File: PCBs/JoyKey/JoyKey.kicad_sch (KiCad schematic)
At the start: 3 parts, among them J1 OLED_DISPLAY, J3 Testpad wire hole1, U3 XIAO-RP2040-DIP

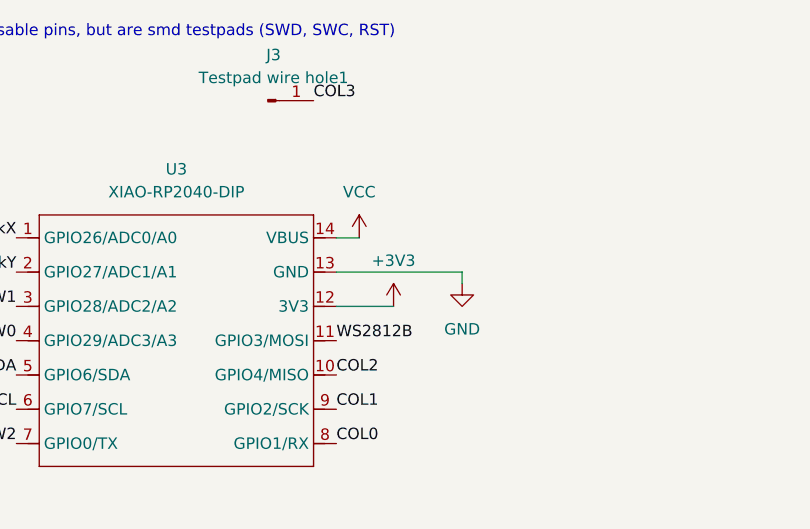
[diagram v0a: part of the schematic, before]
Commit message: Fixed ERC rules
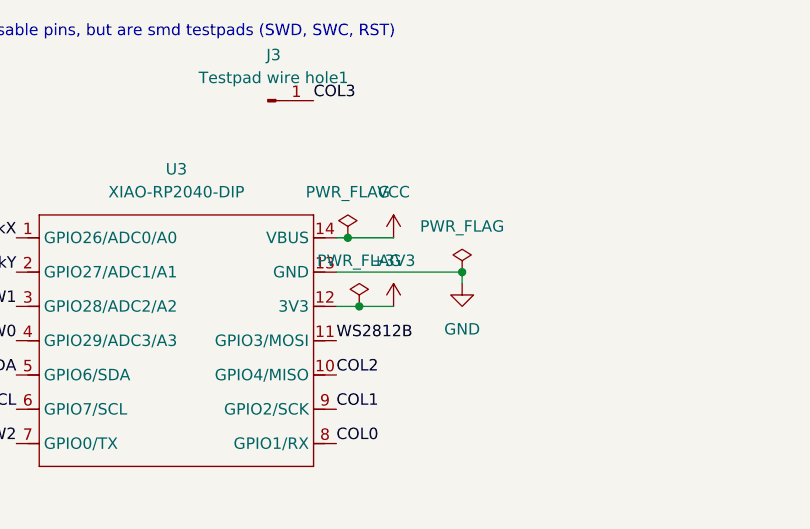
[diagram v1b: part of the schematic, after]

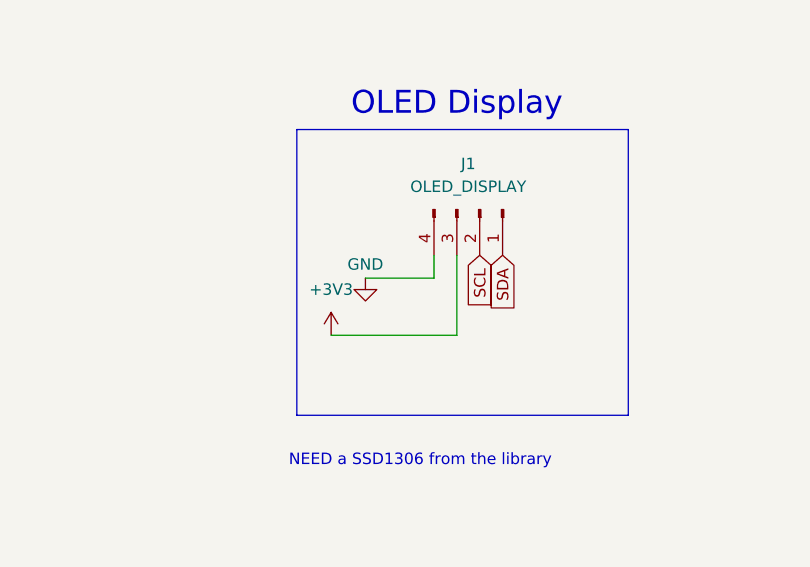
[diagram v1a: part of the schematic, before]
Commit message: Updated display to proper one
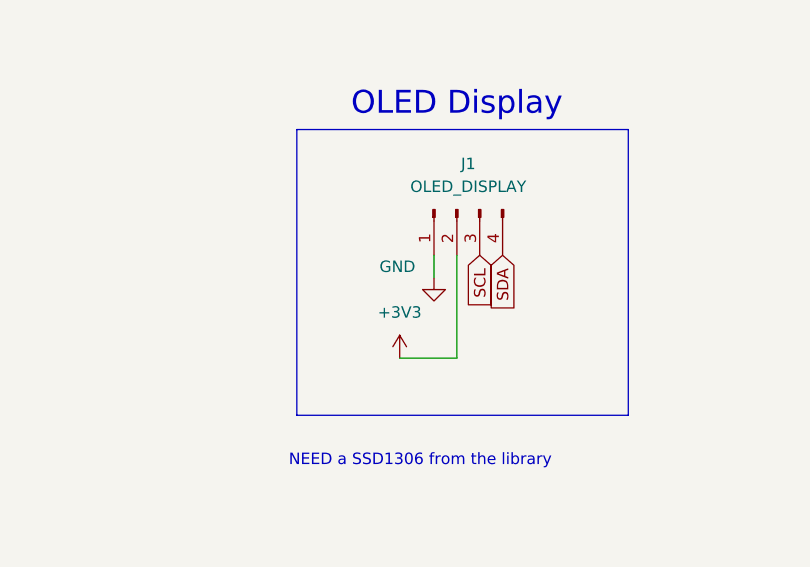
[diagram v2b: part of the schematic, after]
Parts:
- J1: footprint Display:Adafruit_SSD1306 -> SSD1306:SSD1306-OLED096-128x64
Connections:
- net +3V3: now also J1.2 (Pin_2); no longer J1.3 (Pin_3)
- net GND: now also J1.1 (Pin_1); no longer J1.4 (Pin_4)
- net SCL: now also J1.3 (Pin_3); no longer J1.2 (Pin_2)
- net SDA: now also J1.4 (Pin_4); no longer J1.1 (Pin_1)
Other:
- moved on the sheet: J1
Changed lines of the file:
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@@
 	(wire
 		(pts
-			(xy 196.85 66.04) (xy 210.82 66.04)
+			(xy 204.47 68.58) (xy 210.82 68.58)
 		)
 		(stroke
@@
 	(wire
 		(pts
-			(xy 200.66 59.69) (xy 208.28 59.69)
-		)
-		(stroke
-			(width 0)
-			(type default)
-		)
-	)
-	(wire
-		(pts
-			(xy 210.82 66.04) (xy 210.82 57.15)
+			(xy 210.82 68.58) (xy 210.82 57.15)
 		)
 		(stroke
@@
 	(symbol
 		(lib_id "power:GND")
-		(at 200.66 59.69 0)
+		(at 208.28 59.69 0)
 		(unit 1)
 		(exclude_from_sim no)
@@
 		(dnp no)
 		(property "Reference" "#PWR04"
-			(at 200.66 66.04 0)
+			(at 208.28 66.04 0)
 			(effects
 				(font
@@
 		)
 		(property "Value" "GND"
-			(at 200.66 58.166 0)
+			(at 204.216 58.42 0)
 			(effects
 				(font
@@
 		)
 		(property "Footprint" ""
-			(at 200.66 59.69 0)
+			(at 208.28 59.69 0)
 			(effects
 				(font
@@
 		)
 		(property "Datasheet" ""
-			(at 200.66 59.69 0)
+			(at 208.28 59.69 0)
 			(effects
 				(font
@@
 		)
 		(property "Description" "Power symbol creates a global label with name \"GND\" , ground"
-			(at 200.66 59.69 0)
+			(at 208.28 59.69 0)
 			(effects
 				(font
@@
 	(symbol
 		(lib_id "Connector:Conn_01x04_Pin")
-		(at 213.36 52.07 270)
+		(at 210.82 52.07 90)
+		(mirror x)
 		(unit 1)
 		(exclude_from_sim no)
@@
 			)
 		)
-		(property "Footprint" "Display:Adafruit_SSD1306"
-			(at 213.36 52.07 0)
+		(property "Footprint" "SSD1306:SSD1306-OLED096-128x64"
+			(at 210.82 52.07 0)
 			(effects
 				(font
@@
 		)
 		(property "Datasheet" "~"
-			(at 213.36 52.07 0)
+			(at 210.82 52.07 0)
 			(effects
 				(font
@@
 		)
 		(property "Description" "Generic connector, single row, 01x04, script generated"
-			(at 213.36 52.07 0)
+			(at 210.82 52.07 0)
 			(effects
 				(font
@@
 	(symbol
 		(lib_id "power:+3V3")
-		(at 196.85 66.04 0)
+		(at 204.47 68.58 0)
 		(unit 1)
 		(exclude_from_sim no)
@@
 		(fields_autoplaced yes)
 		(property "Reference" "#PWR05"
-			(at 196.85 69.85 0)
+			(at 204.47 72.39 0)
 			(effects
 				(font
@@
 		)
 		(property "Value" "+3V3"
-			(at 196.85 60.96 0)
+			(at 204.47 63.5 0)
 			(effects
 				(font
@@
 		)
 		(property "Footprint" ""
-			(at 196.85 66.04 0)
+			(at 204.47 68.58 0)
 			(effects
 				(font
@@
 		)
 		(property "Datasheet" ""
-			(at 196.85 66.04 0)
+			(at 204.47 68.58 0)
 			(effects
 				(font
@@
 		)
 		(property "Description" "Power symbol creates a global label with name \"+3V3\""
-			(at 196.85 66.04 0)
-			(effects
-				(font
+			(at 204.47 68.58 0)
+			(effects
+				(font

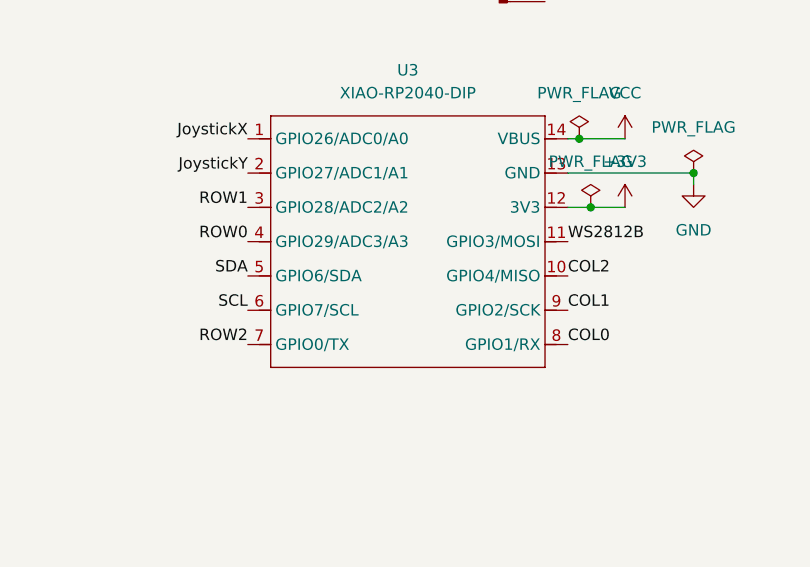
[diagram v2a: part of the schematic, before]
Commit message: Re-arranged matrix to have L-shaped clusters
Based on my horizontal layout I really have a 6*2 matrix, however the most switches for the least pins is actually a 4*3. So, I have to great creative with my routing to make it fit.
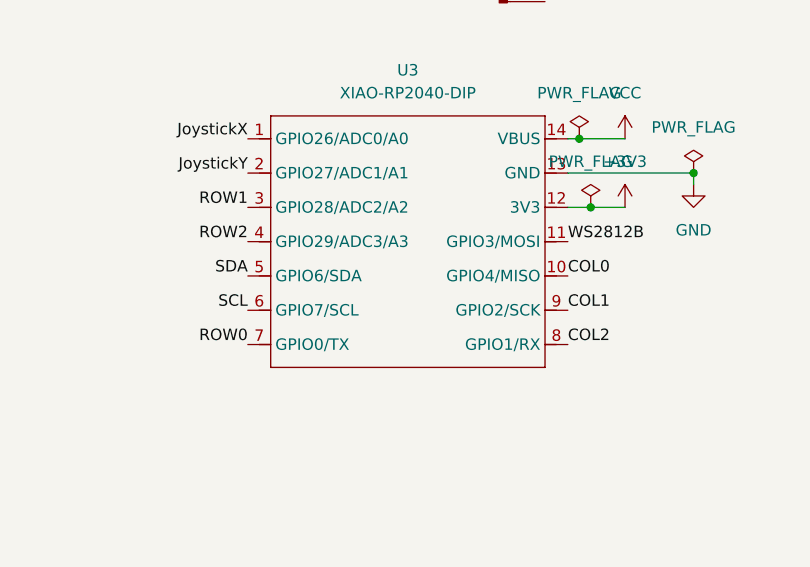
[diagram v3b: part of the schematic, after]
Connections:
- net COL0: now also U3.10 (GPIO4/MISO); no longer U3.8 (GPIO1/RX)
- net COL2: now also U3.8 (GPIO1/RX); no longer U3.10 (GPIO4/MISO)
- net ROW0: now also U3.7 (GPIO0/TX); no longer U3.4 (GPIO29/ADC3/A3)
- net ROW2: now also U3.4 (GPIO29/ADC3/A3); no longer U3.7 (GPIO0/TX)
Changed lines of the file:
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@@
 	)
 	(label "ROW0"
-		(at 102.87 52.07 180)
+		(at 102.87 63.5 180)
 		(effects
 			(font
@@
 	)
 	(label "COL0"
-		(at 138.43 63.5 0)
+		(at 138.43 55.88 0)
 		(effects
 			(font
@@
 	)
 	(label "ROW2"
-		(at 102.87 63.5 180)
+		(at 102.87 52.07 180)
 		(effects
 			(font
@@
 	)
 	(label "COL2"
-		(at 138.43 55.88 0)
+		(at 138.43 63.5 0)
 		(effects
 			(font

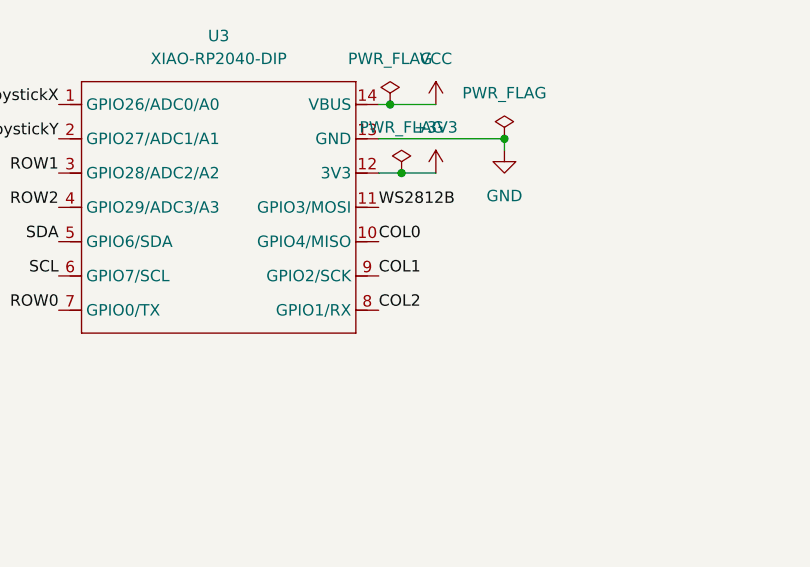
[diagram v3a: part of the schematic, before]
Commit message: Swapped Col1 and 2 for easier routing
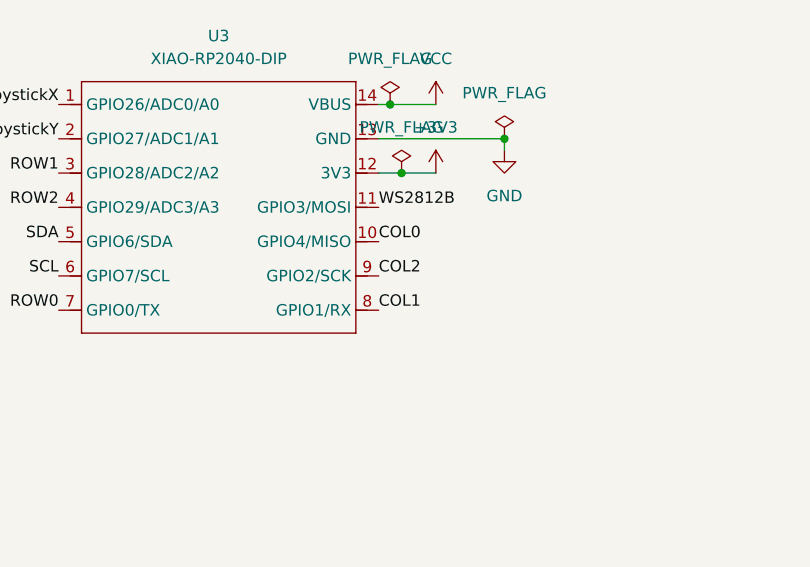
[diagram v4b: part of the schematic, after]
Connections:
- net COL1: now also U3.8 (GPIO1/RX); no longer U3.9 (GPIO2/SCK)
- net COL2: now also U3.9 (GPIO2/SCK); no longer U3.8 (GPIO1/RX)
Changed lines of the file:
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@@
 	)
 	(label "COL1"
-		(at 138.43 59.69 0)
+		(at 138.43 63.5 0)
 		(effects
 			(font
@@
 	)
 	(label "COL2"
-		(at 138.43 63.5 0)
+		(at 138.43 59.69 0)
 		(effects
 			(font

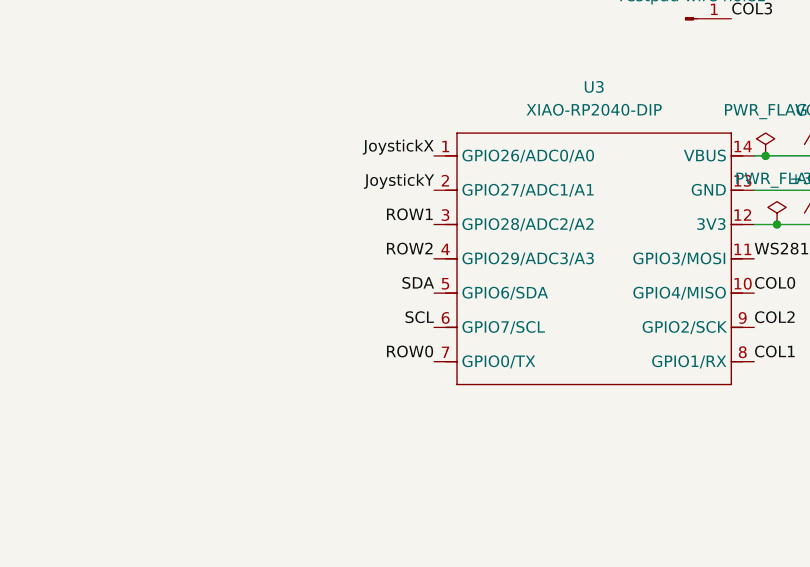
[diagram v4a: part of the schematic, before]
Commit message: Swapped row pins for easier routing
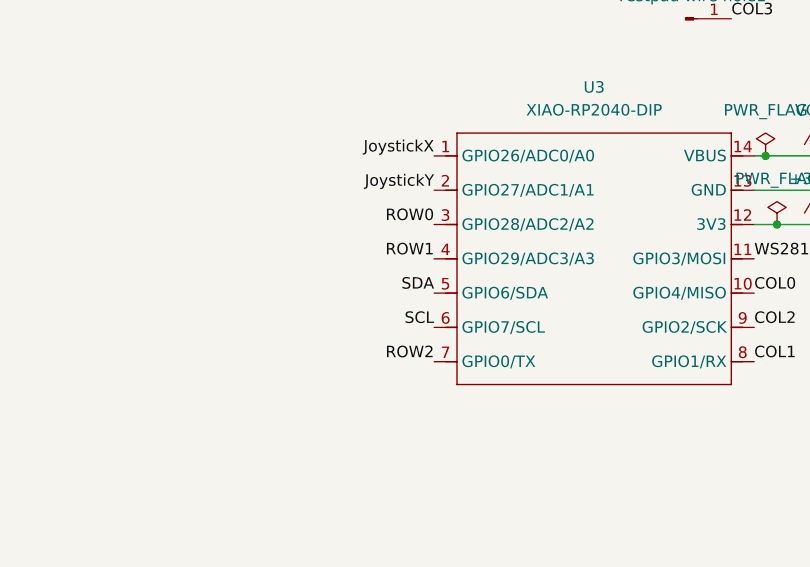
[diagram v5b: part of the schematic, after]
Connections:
- net ROW0: now also U3.3 (GPIO28/ADC2/A2); no longer U3.7 (GPIO0/TX)
- net ROW1: now also U3.4 (GPIO29/ADC3/A3); no longer U3.3 (GPIO28/ADC2/A2)
- net ROW2: now also U3.7 (GPIO0/TX); no longer U3.4 (GPIO29/ADC3/A3)
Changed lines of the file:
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@@
 	)
 	(label "ROW1"
-		(at 102.87 48.26 180)
+		(at 102.87 52.07 180)
 		(effects
 			(font
@@
 	)
 	(label "ROW0"
-		(at 102.87 63.5 180)
+		(at 102.87 48.26 180)
 		(effects
 			(font
@@
 	)
 	(label "ROW2"
-		(at 102.87 52.07 180)
+		(at 102.87 63.5 180)
 		(effects
 			(font

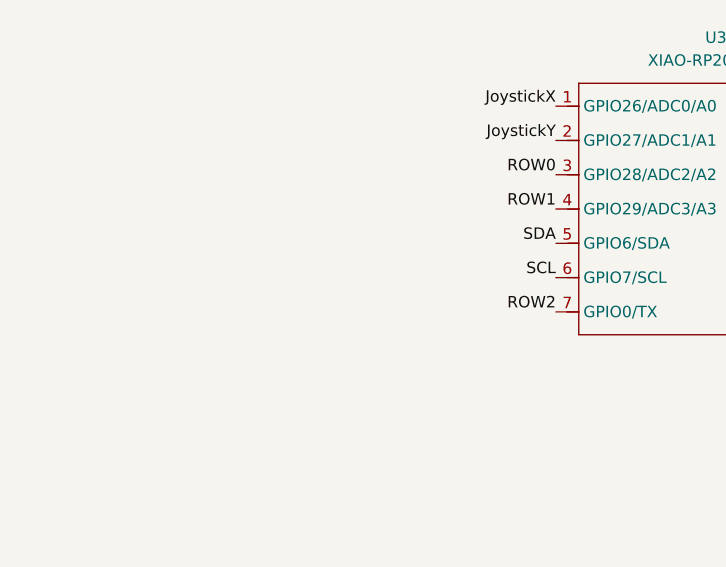
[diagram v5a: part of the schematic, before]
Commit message: Add 2 mounting holes
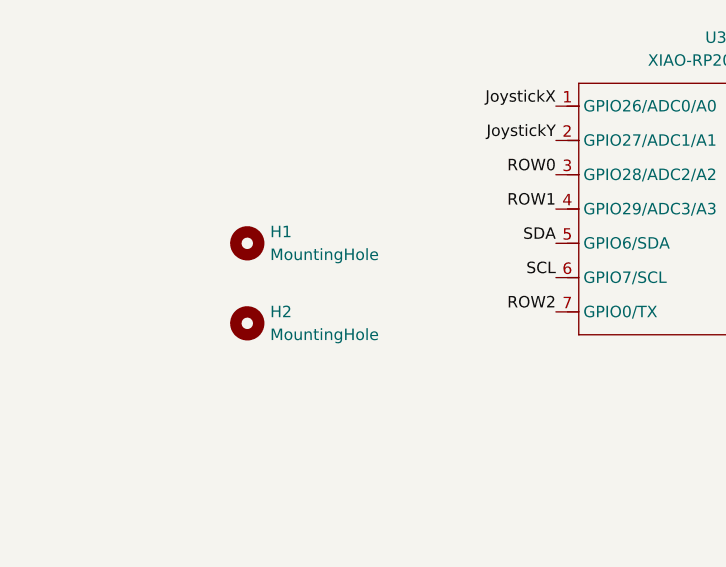
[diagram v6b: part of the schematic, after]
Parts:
- added H1, H2: MountingHole, MountingHole:MountingHole_3.2mm_M3_Pad, symbol Mechanical:MountingHole
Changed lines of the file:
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@@
+	)
+	(symbol
+		(lib_id "Mechanical:MountingHole")
+		(at 68.58 55.88 0)
+		(unit 1)
+		(exclude_from_sim yes)
+		(in_bom no)
+		(on_board yes)
+		(dnp no)
+		(fields_autoplaced yes)
+		(property "Reference" "H1"
+			(at 71.12 54.6099 0)
+			(effects
+				(font
+					(size 1.27 1.27)
+				)
+				(justify left)
+			)
+		)
+		(property "Value" "MountingHole"
+			(at 71.12 57.1499 0)
+			(effects
+				(font
+					(size 1.27 1.27)
+				)
+				(justify left)
+			)
+		)
+		(property "Footprint" "MountingHole:MountingHole_3.2mm_M3_Pad"
+			(at 68.58 55.88 0)
+			(effects
+				(font
+					(size 1.27 1.27)
+				)
+				(hide yes)
+			)
+		)
+		(property "Datasheet" "~"
+			(at 68.58 55.88 0)
+			(effects
+				(font
+					(size 1.27 1.27)
+				)
+				(hide yes)
+			)
+		)
+		(property "Description" "Mounting Hole without connection"
+			(at 68.58 55.88 0)
+			(effects
+				(font
+					(size 1.27 1.27)
+				)
+				(hide yes)
+			)
+		)
+		(instances
+			(project ""
+				(path "/7995ec7a-c14b-437e-b354-3eb74052b7cb"
+					(reference "H1")
+					(unit 1)
+				)
+			)
+		)
 	)
 	(symbol
@@
 					(unit 1)
 				)
+			)
+		)
+	)
+	(symbol
+		(lib_id "Mechanical:MountingHole")
+		(at 68.58 64.77 0)
+		(unit 1)
+		(exclude_from_sim yes)
+		(in_bom no)
+		(on_board yes)
+		(dnp no)
+		(fields_autoplaced yes)
+		(property "Reference" "H2"
+			(at 71.12 63.4999 0)
+			(effects
+				(font
+					(size 1.27 1.27)
+				)
+				(justify left)
+			)
+		)
+		(property "Value" "MountingHole"
+			(at 71.12 66.0399 0)
+			(effects
+				(font
+					(size 1.27 1.27)
+				)
+				(justify left)
+			)
+		)
+		(property "Footprint" "MountingHole:MountingHole_3.2mm_M3_Pad"
+			(at 68.58 64.77 0)
+			(effects
+				(font
+					(size 1.27 1.27)
+				)
+				(hide yes)
+			)
+		)
+		(property "Datasheet" "~"
+			(at 68.58 64.77 0)
+			(effects
+				(font
+					(size 1.27 1.27)
+				)
+				(hide yes)
+			)
+		)
+		(property "Description" "Mounting Hole without connection"
+			(at 68.58 64.77 0)
+			(effects
+				(font
+					(size 1.27 1.27)
+				)
+				(hide yes)
+			)
+		)
+		(instances
+			(project "JoyKey"
+				(path "/7995ec7a-c14b-437e-b354-3eb74052b7cb"
+					(reference "H2")
+					(unit 1)
+				)
